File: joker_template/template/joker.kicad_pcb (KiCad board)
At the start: 2 copper layers, 19 parts, among them U1 BL24C256A-SFRC, U2 STM32F411CEU6, Y1 7325-0800A2010-00

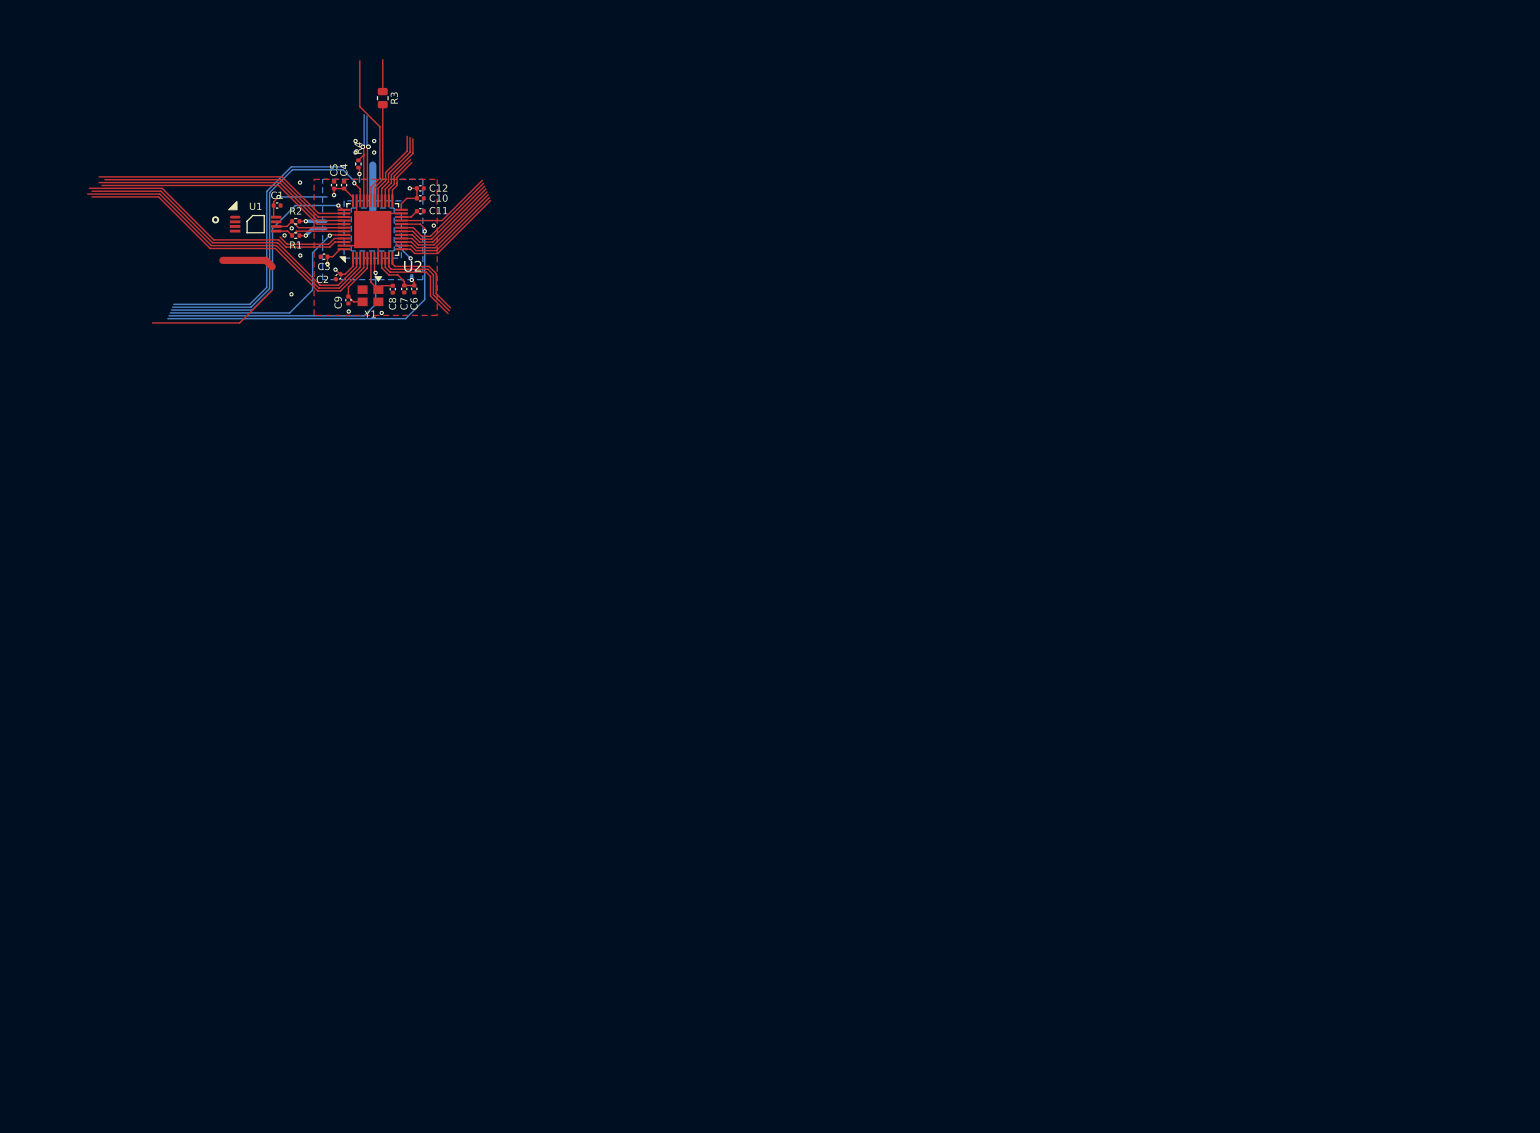
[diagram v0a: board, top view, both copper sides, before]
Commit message: New makefile version for joker template
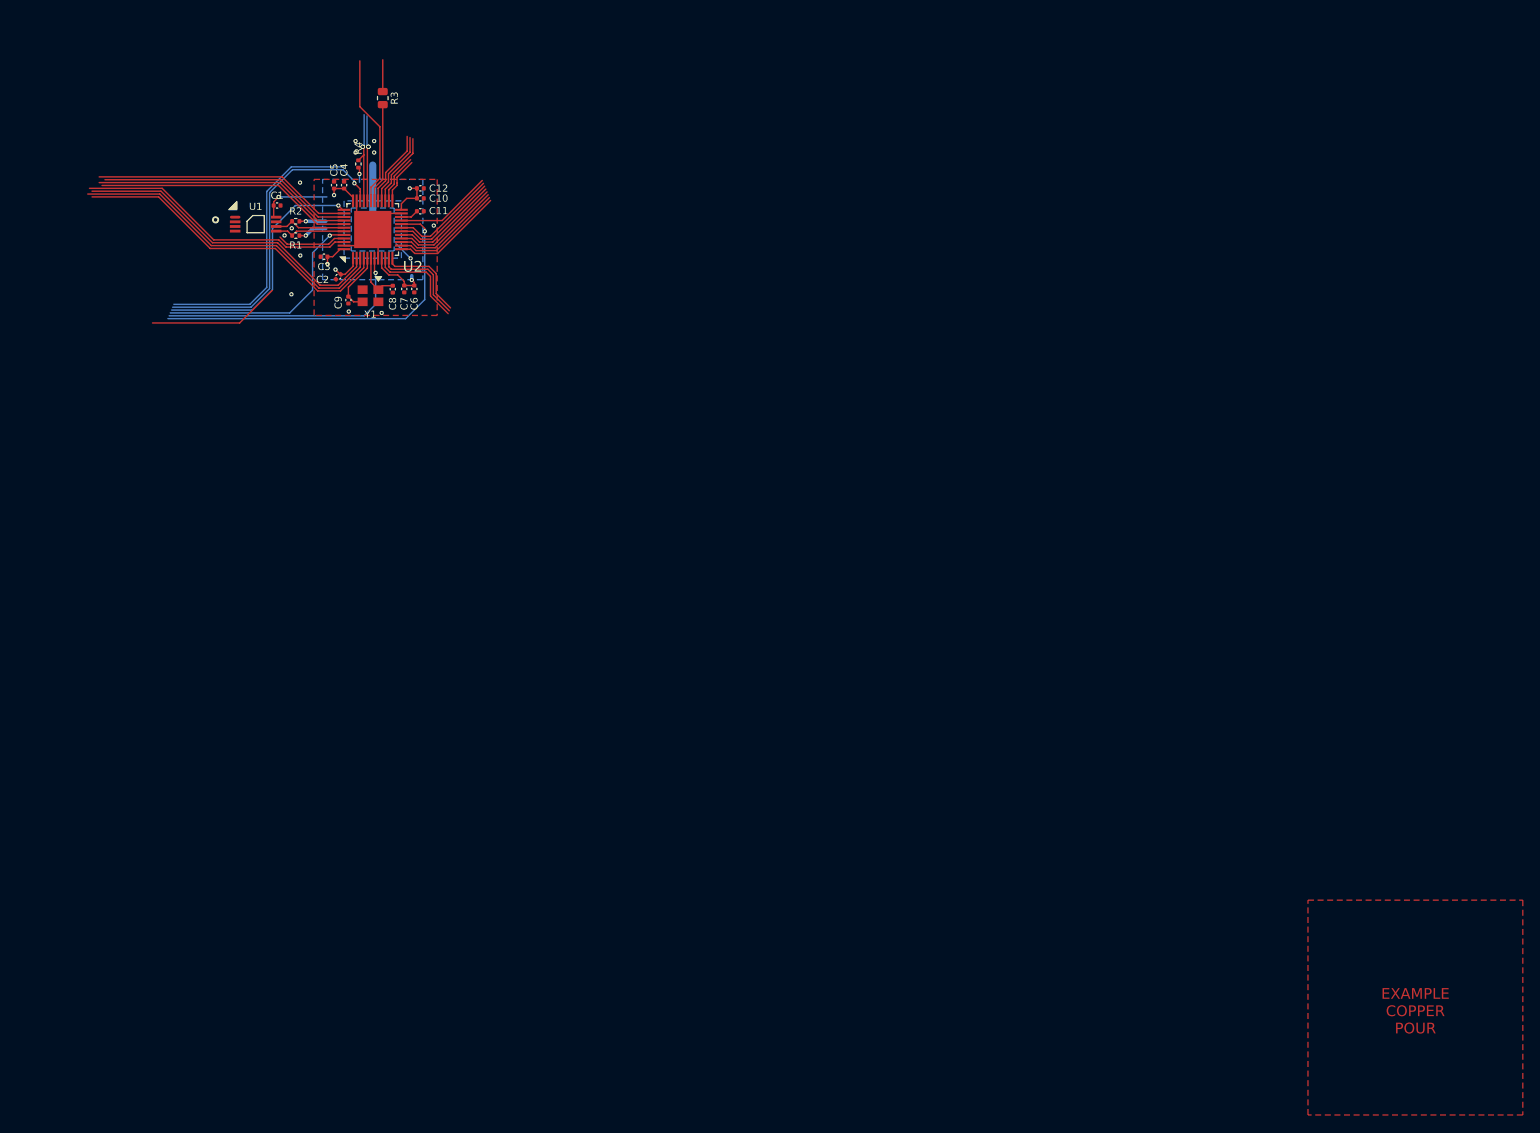
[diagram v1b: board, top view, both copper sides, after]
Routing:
- net (no net): track 7.27 -> 0.00 mm
- added copper zone on F.Cu, net (none)
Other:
- board text added: "(1) Make liberal use of the F.Fab and B.Fab layers. Those should be used for documentation which you want to relay to your fab house. Component pinage"
- board text added: "(1) USB DATA TRACES: make sure to route them as short as possible, parallel to one another. Also learn to use the phase skew adjustment tool of KiCAD. Avoid"
- board text added: "(2) CRYSTAL TRACES: these are the highest frequency traces on the PCB and should be handled with extreme care. Always place the crystal extremely close to"
- board text added: "(2) Treat the silkscreen layers with very good care. Make sure that the component designators are minimally sized (1mm tall with 0.2mm trace width is advised),"
- board text added: "(3) BYPASS CAPACITORS: the precise function and nature of bypass (also called decoupling) capacitors is difficult to explain without higher knowledge in maths"
- board text added: "(3) KiCAD allows custom user layers. Use those to indicate screw hole anchors/sizes, plate markings, stabilizer orientation. Document everything because"
- board text added: "(4) If you want to share or open-source your design, be kind and make sure all your thought process or ideas are clearly documented and defined. Revising"
- board text added: "(5) Yes, documenting is boring. Everyone knows that, and yet everyone takes the time to do it because it saves you time and headaches down the line."
- board text added: "(also known as relief cuts) or leaf-spring mounting points."
- board text added: "- If you are beggining on PCB design or are using a new fab, it might be wise to just use the values here for now"
- board text added: "- Manufacturing parameters might change in which case the tolerance values will change accordingly"
- board text added: "- Recommended are the smalles tolerances doable with no fabrication or quality control issues. These can be safely used without incurring in higher costs"
- board text added: "- Such values *should* be enough for keyboard PCBs"
- board text added: "- The values used are based on experience but should be manufacturable at low cost and accepted industry-wide"
- board text added: "- You can freely change these parameters around but make sure what those changes entail to, cost and production-wise"
- board text added: "- {dblquote}Factory{dblquote} are the values minimally feasible needed by factories. Different ones will inevitably have different numbers, but through using multiple a common"
- board text added: "0.05"
- board text added: "0.13"
- board text added: "0.15 (see [i])"
- board text added: "0.2 (see [1])"
- board text added: "0.3 (see [iii])"
- board text added: "0.4"
- board text added: "0.5 (see [iv])"
- board text added: "0.8"
- board text added: "1:5 (see [v])"
- board text added: "1:6 (see [ii])"
- board text added: "A change in manufacturing parameters (layers and copper weight) will unequivocaly change the minimum values."
- board text added: "Adjust the values at your own discretion, but be very mindful of these tolerances as they are imperative for the manufacturing process and feasibility of the final PCB."
- board text added: "At the bottom-right of the page there is a copper polygon with the settings generally used for the Acheron Project. The values are tuned for general use, but"
- board text added: "Avoid using hatched-pattern copper pours. They have their reason to be, but not on keyboard PCBs. They are ugly (yeah, fight me) and don't do what we want them"
- board text added: "DO NOT use these values in other settings; always coordinate properly with the factory for that."
- board text added: "EXAMPLE COPPER POUR"
- board text added: "Elecrow offers {dblquote}standard PCB{dblquote} and {dblquote}advanced PCB{dblquote} services ([2]), while PCBWay offers {dblquote}normal difficulty{dblquote}, {dblquote}medium difficulty{dblquote} and {dblquote}high difficulty{dblquote} processes ([3])"
- board text added: "Even though keyboard PCB design is very forgiving in terms of the mistakes and errors you can make, there are some problems that are potentially PCB-breaking."
- board text added: "FACTORY MINIMUMS"
- board text added: "For clarification, read the NOTES ON TOLERANCES."
- board text added: "For requests/issues please submit a issue in the github folder. Do not attempt to contact the developers directly."
- board text added: "For the actual values, check references [1-3]."
- board text added: "IMPORTANT"
- board text added: "In both manufacturers, the advanced settings have smaller tolerances and better manufacturing features but are significantly more expensive, specially"
- board text added: "It is offered under a no-liability, as-is clause. Please visit http://github.com/AcheronProject/AcheronSetup for more information."
- board text added: "It must also be kept in mind that, since the Acheron Project is heavily DIY-oriented, the tolerance settings used were the easiest or cheapest available. For instance,"
- board text added: "Keep in mind that these are, after all, minimum values. Always try to stray away from them when there is chance, so as to give you and the factory headroom to work with."
- board text added: "LEDs and level shifters. Treat bypass capacitors like you would a crystal: as close to the main device as possible and with short traces. Always look at"
- board text added: "Many DIY designers will state that the usage of copper pours is perfeccionism; in some cases, designers will argue that the pours are actually detrimental to the design"
- board text added: "NOTES"
- board text added: "NOTES ON COPPER POURS"
- board text added: "NOTES ON TOLERANCES"
- board text added: "OVERALL DESIGN RECOMMENDATIONS"
- board text added: "PCB design involves a lot of creativity and not everyone understands your codes and conventions. Take good care of documenting your PCB. Some tips:"
- board text added: "PLEASE READ"
- board text added: "Please note that the files need such libraries to fully work."
- board text added: "RECOMMENDED MINIMUMS"
- board text added: "REFERENCES"
- board text added: "Sharing your design and knowledge is one of the most fruitful and effective ways to learn design and gain knowledge. Look at other people's designs and frequently"
- board text added: "TLDR"
- board text added: "The actually used values can very well vary according to your specifications and the capabilities of the factory being used."
- board text added: "The files generated are compatible with KiCAD developmental ({dblquote}nightly{dblquote}) versions up to august 16, 2021 version."
- board text added: "The first experience with PCB design is always very frustrating and overwhelming. There will be a lot of failed prototypes before you consider yourself a minimally"
- board text added: "The manufacturing tolerances used for PCBs in the Acheron Project are a way to uniformize the design settings of the projects. These settings were obtained using"
- board text added: "The most common problems for first-timers in keyboard PCB design are (1) USB data traces routing (2) crystal traces routing and (3) bypass capacitors placement"
- board text added: "The tolerances used might seem too loose or big, but these are the bare large-scale manufacturable values found through experience using multiple factories."
- board text added: "The values and observations here listed consider a two-layer, 1 oz/ft2 PCB"
- board text added: "The values used divide into two groups: the {dblquote}factory minimums {dblquote} and the {dblquote}recommended minimum{dblquote} ones."
- board text added: "Therefore even for a 2-layer 1oz/ft2 PCB tolerances can be different for the {dblquote}advanced{dblquote} or {dblquote}high-difficulty{dblquote} settings."
- board text added: "Therefore, it must always be understood that a single body of uniform tolerances throughout a wide spectrum of projects is unfeasible due to the very nature"
- board text added: "These files should also be accompanied of a librires folder where the used libraries are added as submodules which last commit should point to the remote's HEAD."
- board text added: "This PCB file was generated through the Acheron Setup script, an automated tool to generate design-ready KiCAD schematic and PCB files for keyboard projects."
- board text added: "USAGE COMMENTS"
- board text added: "Use copper pours are your discretion but I (Gondolindrim) recommend always using them. My designs make liberal use of such pours even for other signals."
- board text added: "Values also pertain to the cheapest setting on the referenced manufacturers."
- board text added: "We ask that bugs/problems be reported through the issues page too."
- board text added: "Yes I know it's a lot of stuff but please read, it's important I promise"
- board text added: "You can safely delete this message, as long as you keep these comments in mind while using these files."
- board text added: "You should read it all though"
- board text added: "[1] PCBWay manufacturing capabilities. Link: <https://www.pcbway.com/capabilities.html>. Last access august 21, 2021."
- board text added: "[2] JLCPCB manufacturing capabilities. Link: <https://jlcpcb.com/capabilities/Capabilities>. Last accessed august 21, 2021."
- board text added: "[3] Elecrow manufacturing capabilities. Link: <https://www.elecrow.com/download/quote/PCB_Specification_FAQ.pdf> . Last access august 21, 2021."
- board text added: "[4] Sanjeeb Mishra, Neeraj Kumar Singh, Vijayakrishnan Rousseau. System on Chip Interfaces for Low Power Design. Morgan Kaufmann, 2016. ISBN 9780128016305. Accessible via https://www.sciencedirect.com/science/article/pii/B9780128016305000104)"
- board text added: "[5] Seeedstudio manufacturing capabilities. Link: <https://support.seeedstudio.com/knowledgebase/articles/447362-fusion-pcb-specification> . Last accessed august 21, 2021."
- board text added: "[i] Official copper-copper clearances are 0.2mm but not exactly {dblquote}all copper{dblquote}. Pad-to-pad minimums are 0.5mm in the case of THT pads and 0.2mm for SMD pads."
- board text added: "[ii] The recommended ratio between silkscreen character height and its trace width so they are clearly legible."
- board text added: "[iii] The hole-to-copper clearance changes on occasion. For instance, via-to-track and NPTH-to-track clearance is 0.25mm but PTH-to-track is 0.3."
- board text added: "[iv] The distance of copper-to-edge is a big problem for fabs in designs where traces need to be close to certain slots or the edges, like keyboard PCBs with flex cuts"
- board text added: "[v] The 1:6 ratio for silkscreen is OK for large characters but can become unreadable to the naked eye on a 1mm character. A 1:5 ratio is recommended."
- board text added: "a PCB, much like a computer code or a maths test, requires knowledge that is either a convention or only the author knows."
- board text added: "adjustments can be made. Thermal spoke width and relief gap can be adjusted according to the thermal needs -- for THT components or connectors, it is"
- board text added: "and engineering. In layman's terms, bypass capacitors are placed to mitigate noise inherently present in digital circuits due to the natural inductance"
- board text added: "and polarity, values, designators, everything goes to make the fab's job easier -- and yours in the process."
- board text added: "and requirements of the different PCB projects. The values suggested here used in these files are only *recommendations* based on experience, having been"
- board text added: "and routing. In this order, they are the most problematic parts of designing a keyboard PCB and are the most frequent issues."
- board text added: "are proven to work."
- board text added: "breaking and VIA'ing them as much as possible. If those are needed, do so in a simmetrical manner. If also possible, please read on differential pair"
- board text added: "communication (see [4], pages 331-344)."
- board text added: "datasheets, reference manuals and application notes which will generally inform how many capacitors are needed and their respective values and sizes."
- board text added: "denominator was found. These values should not be used often, but seldomly at the designer's discretion and in ultimate case. Their use will incurr in higher"
- board text added: "does not accompany its files; when someone looks at the PCB, component designators and polarities should be very clear and direct."
- board text added: "electronics and embedded systems is also recommended, but higher education in maths and engineering is absolutely not needed to be a DIY designer."
- board text added: "good PCB designer, and there is always something to learn. Since PCB design is a highly technical and skill-oriented field, it can sometimes looks as"
- board text added: "high-density designs etc) and are completely unnecessary for keyboard projects."
- board text added: "in keyboard PCBs, however, the copper pours make the PCBs stiffer, reducing what is known as {dblquote}flex{dblquote}. The way to countermeasure that is by deploying flex cuts"
- board text added: "in the eventuality you want to make a revision or correction, all the information is in the files and not somewhere else buried deep down in emails"
- board text added: "mainly three manufacturers: PCBWay, Elecrow and JLCPCB (see their capabilities pages on references [1-3]). These are big players in the asian PCB manufacturing"
- board text added: "manufacturing fees, larger lead times, more quality check issues (PCBs failing after large production)."
- board text added: "market and the tolerances practiced by them are accepted industry-wide; hence, the values used here should be enough for most manufacturers."
- board text added: "of traces and the switching characteristic of digital circuitry. Failure to properly place and route these capacitors can lead to inability of the digital circuits"
- board text added: "or Discord conversations."
- board text added: "or major large-scale production issues. There is no particular reason for any of these but experience through usage of many factories. This KiCAD file"
- board text added: "recommended to use higher gaps (0.5mm will do the trick) to avoid bad solder joints."
- board text added: "since most (if not all) modern keyboards work under USB communication which uses differential pair topology, a ground copper pour is absolutely needed"
- board text added: "some sorte of black magic. Do not stray from resilience. The best way to learn PCB design is designing. Some study in the fundamental aspects of"
- board text added: "talk to other designers. This ensures a collective knowledge is achieved both in hard and soft skills."
- board text added: "the MCU (in its vicinities) and if possible sharing the same ground (ideally islanded)."
- board text added: "to do here. Always use solid fills. The drawback is that they can make the PCB stiffer, so use flex cuts on the PCB."
- board text added: "to ensure proper return currents paths, low ground impedance, EMI resistance, efficiency in ESD protection, protection from overheating, and so on. Particularly"
- board text added: "to work properly. In the specific case of keyboard PCBs, there are plenty of digital circuits that need decoupling, mainly the microcontroller, RGB underglow"
- board text added: "used in a myriad of projects throughout the Acheron Project and in Gondolindrim's personal and professional projects."
- board text added: "visible. Also make sure that the silkscreen indicates the polarity of components either through arrows or symbols. Remember that the physical PCB"
- board text added: "was set to use the recommended values in its Design Rule Checks and routines; these values were used successfully throughout the Acheron Project and"
- board text added: "when paired with PCB assembly services. Such settings are meant for more complex projects (high-speed or analog signal processing, finer electronic components,"
- board text added: "where the PCB traces need to be routed close to the flex cuts for lack of real-estate. This is why this value is much higer than the fabrication ones."
- board text added: "while I (gondolindrim) disagree with the former I agree with the latter in some respects. Ground pours are an integral part of digital high-speed signal design;"
- board text removed: "1:5"
- board text removed: "1oz per ft2"
- board text removed: "DOUBLE-SIDED TWO LAYERS"
- board text removed: "PCB COPPER WEIGHT:"
- board text removed: "PCB LAYERS:"

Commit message: New version of joker template
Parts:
- added X1: ARM JTAG, acheron_Connectors:PinHeader_2x5_P2.54mm_Vertical_Staggered, F.Cu at (215.1, 137.4)
- U2: footprint acheron_Components:STM_UFQFPN-48_LQFP-48-1EP_7x7mm_P0.5mm_HandSoldering -> acheron_Components:STM_UFQFPN-48_LQFP-48-1EP_7x7mm_P0.5mm_HandSoldering_ThermalReliefs
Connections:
- net C5 renamed LED_PWM
- net PA9 renamed /PA9
- net PB15 renamed RGB_3V3
- U2 pad 10: R4 -> unconnected-(U2-Pad10)
- U2 pad 11: C2 -> unconnected-(U2-Pad11)
- U2 pad 12: C1 -> unconnected-(U2-Pad12)
- U2 pad 13: C0 -> unconnected-(U2-Pad13)
- U2 pad 14: R0 -> unconnected-(U2-Pad14)
- U2 pad 15: R1 -> unconnected-(U2-Pad15)
- U2 pad 17: C4 -> unconnected-(U2-Pad17)
- U2 pad 18: C3 -> unconnected-(U2-Pad18)
- U2 pad 2: C14 -> unconnected-(U2-Pad2)
- U2 pad 21: R2 -> unconnected-(U2-Pad21)
- U2 pad 25: PB12 -> unconnected-(U2-Pad25)
- U2 pad 26: PB13 -> unconnected-(U2-Pad26)
- U2 pad 27: PB14 -> unconnected-(U2-Pad27)
- U2 pad 29: PA8 -> unconnected-(U2-Pad29)
- U2 pad 3: C13 -> unconnected-(U2-Pad3)
- U2 pad 31: R3 -> unconnected-(U2-Pad31)
- U2 pad 38: C11 -> unconnected-(U2-Pad38)
- U2 pad 39: C10 -> unconnected-(U2-Pad39)
- U2 pad 4: C12 -> unconnected-(U2-Pad4)
- U2 pad 40: C9 -> unconnected-(U2-Pad40)
- U2 pad 41: C8 -> unconnected-(U2-Pad41)
- U2 pad 45: C6 -> unconnected-(U2-Pad45)
- U2 pad 46: C7 -> unconnected-(U2-Pad46)
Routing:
- net unconnected-(U2-Pad4): track 0.00 -> 46.1 mm
- net C12: track 46.1 -> 0.00 mm
- net unconnected-(U2-Pad3): track 0.00 -> 46.0 mm
- net C13: track 46.0 -> 0.00 mm
- net unconnected-(U2-Pad2): track 0.00 -> 44.7 mm
- net C14: track 44.7 -> 0.00 mm
- net unconnected-(U2-Pad46): track 0.00 -> 39.2 mm
- net C7: track 39.2 -> 0.00 mm
- net unconnected-(U2-Pad40): track 0.00 -> 36.4 mm
- net C9: track 36.4 -> 0.00 mm
- net unconnected-(U2-Pad38): track 0.00 -> 36.3 mm
- net C11: track 36.3 -> 0.00 mm
- net unconnected-(U2-Pad41): track 0.00 -> 36.0 mm
- net C8: track 36.0 -> 0.00 mm
- net unconnected-(U2-Pad39): track 0.00 -> 35.6 mm
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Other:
- board outline added: 80 x 60 mm
- board text added: "3V3"
- board text added: "BOOT0"
- board text added: "BOOT1"
- board text added: "GND"
- board text added: "It is offered under a no-liability, as-is clause. Please visit http://github.com/AcheronProject/AcheronSetup/joker_template for more information."
- board text added: "READ THE DOCUMENTATION."
- board text added: "SWCLK"
- board text added: "SWD"
- board text added: "SWDIO"
- board text added: "The files generated are compatible with KiCAD developmental ({dblquote}nightly{dblquote}) versions up to sptember 9, 2021 version."
- board text added: "This PCB file was generated by the Acheron Setup script Joker template, an automated tool to generate design-ready KiCAD schematic and PCB files for keyboard projects."
- board text added: "Whether you are using these files for a hobby project or plan to use it for actually selling PCBs, you MUST know what you are using and getting yourself into. Read the notes, the documentation and understand it fully. You may remove this message."
- board text added: "nRST"
- board text removed: "It is offered under a no-liability, as-is clause. Please visit http://github.com/AcheronProject/AcheronSetup for more information."
- board text removed: "The files generated are compatible with KiCAD developmental ({dblquote}nightly{dblquote}) versions up to august 16, 2021 version."
- board text removed: "This PCB file was generated through the Acheron Setup script, an automated tool to generate design-ready KiCAD schematic and PCB files for keyboard projects."
